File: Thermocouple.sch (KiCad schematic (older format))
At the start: 22 parts, among them P2 CONN_2, P3 CONN_3X2, U10 MCP3901, U11 LMT84, U4 OPA4170

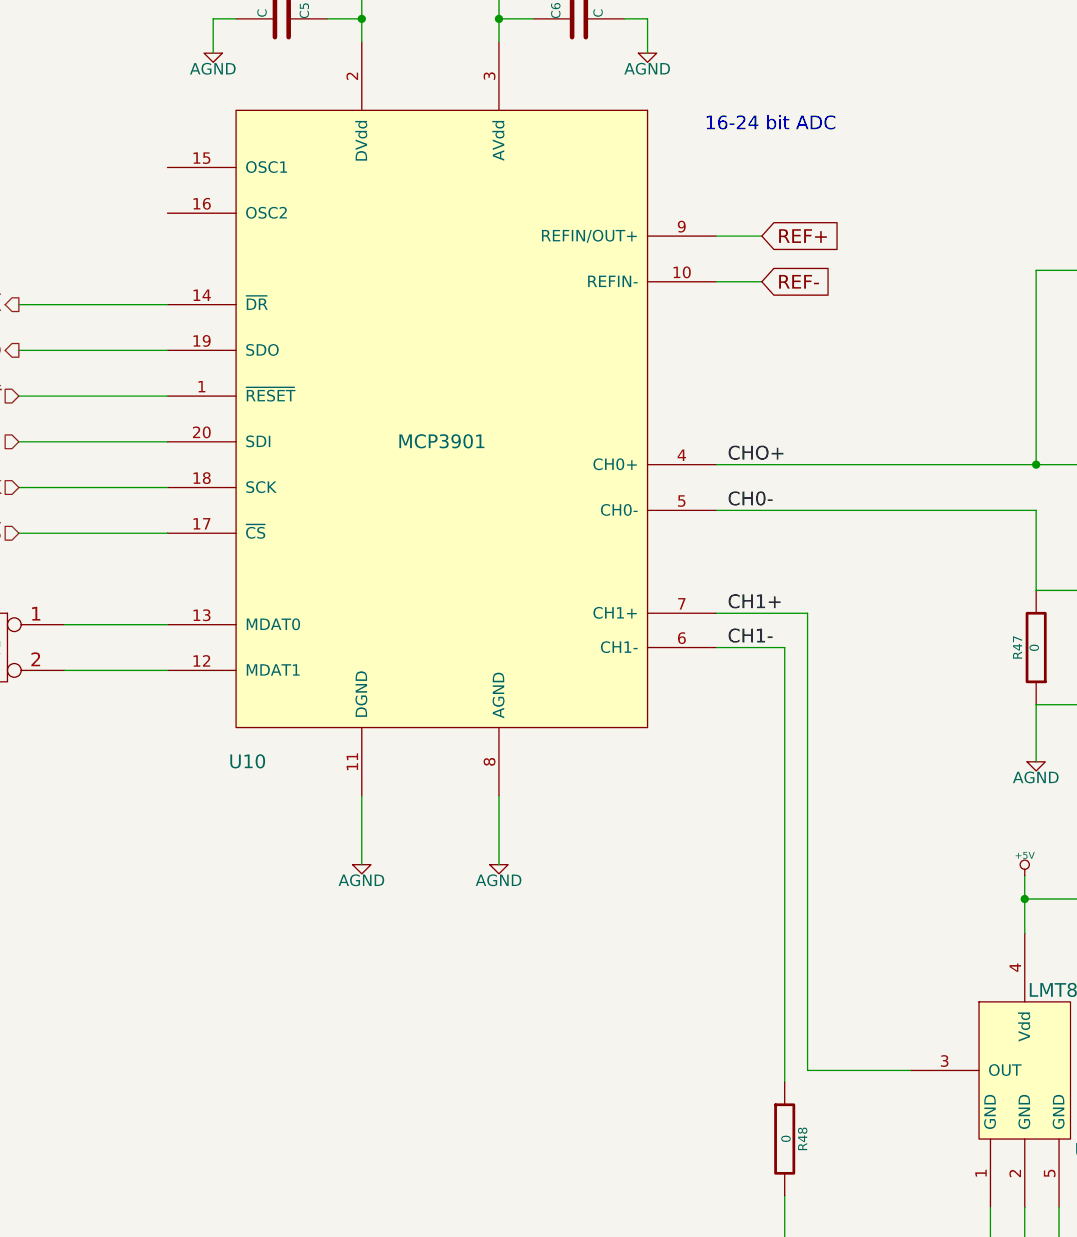
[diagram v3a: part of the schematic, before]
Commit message: Cleanup/ERC checks, etc (on my own, no video)
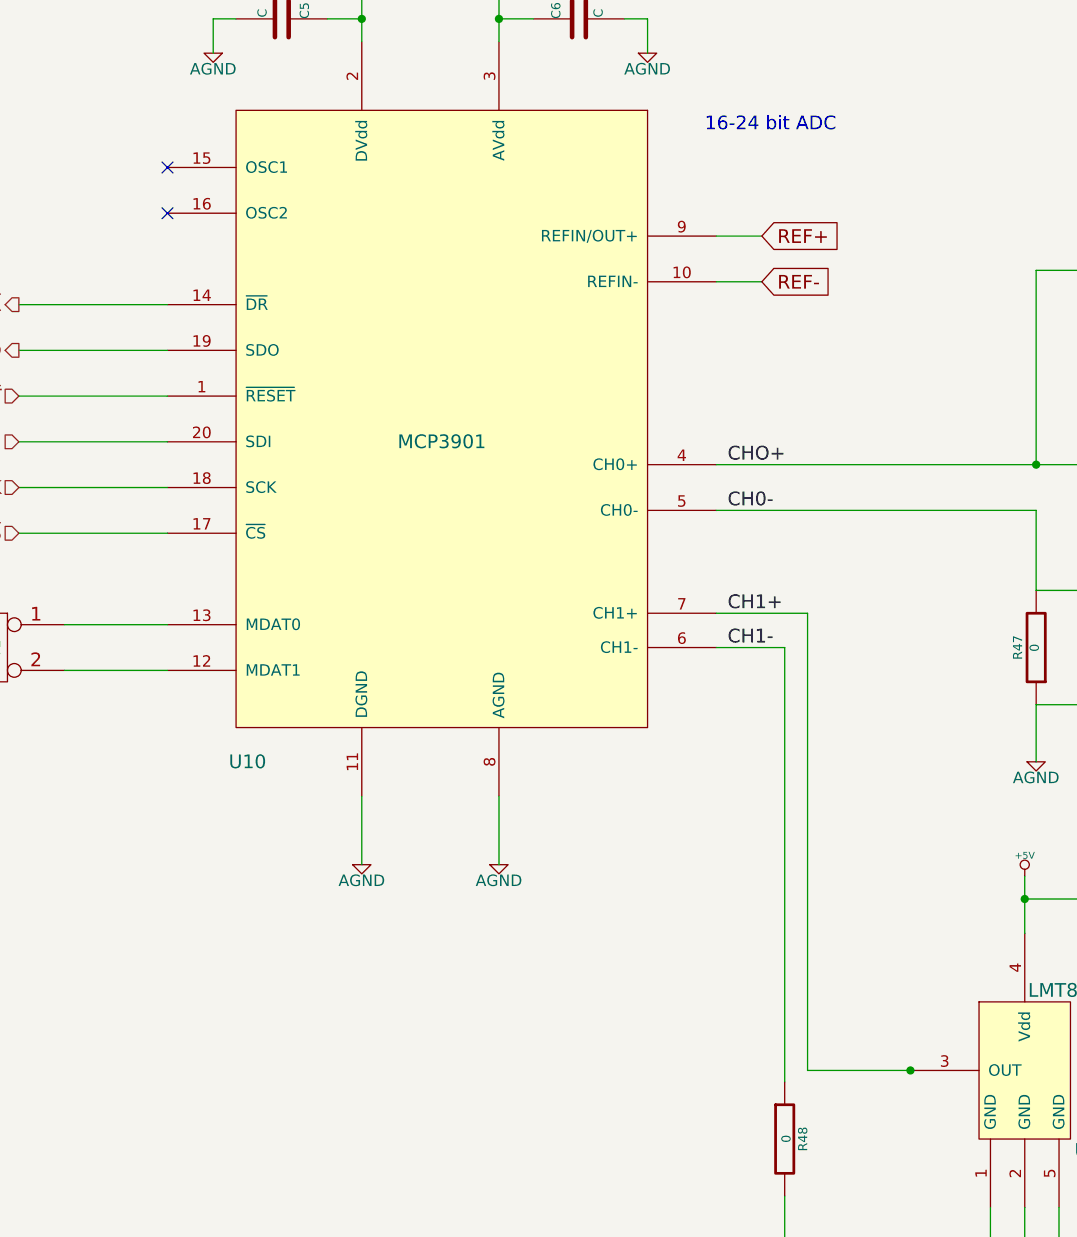
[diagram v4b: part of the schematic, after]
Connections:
- no-connect marks 0 -> 2
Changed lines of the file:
@@
 	8050 2750 8050 2650
 Connection ~ 8050 2100
+NoConn ~ 1600 1650
+NoConn ~ 1600 1850
+Connection ~ 4850 5600
 $EndSCHEMATC
